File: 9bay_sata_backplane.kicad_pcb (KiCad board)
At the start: 2 copper layers, 115 x 58 mm, 57 parts, among them J1 Screw_Terminal_01x04, U1 SATA_Connector, U10 SATA_Data, U11 SATA_Data, U12 SATA_Data, U13 SATA_Data, U14 SATA_Data, U15 SATA_Data, U16 SATA_Data, U17 SATA_Data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

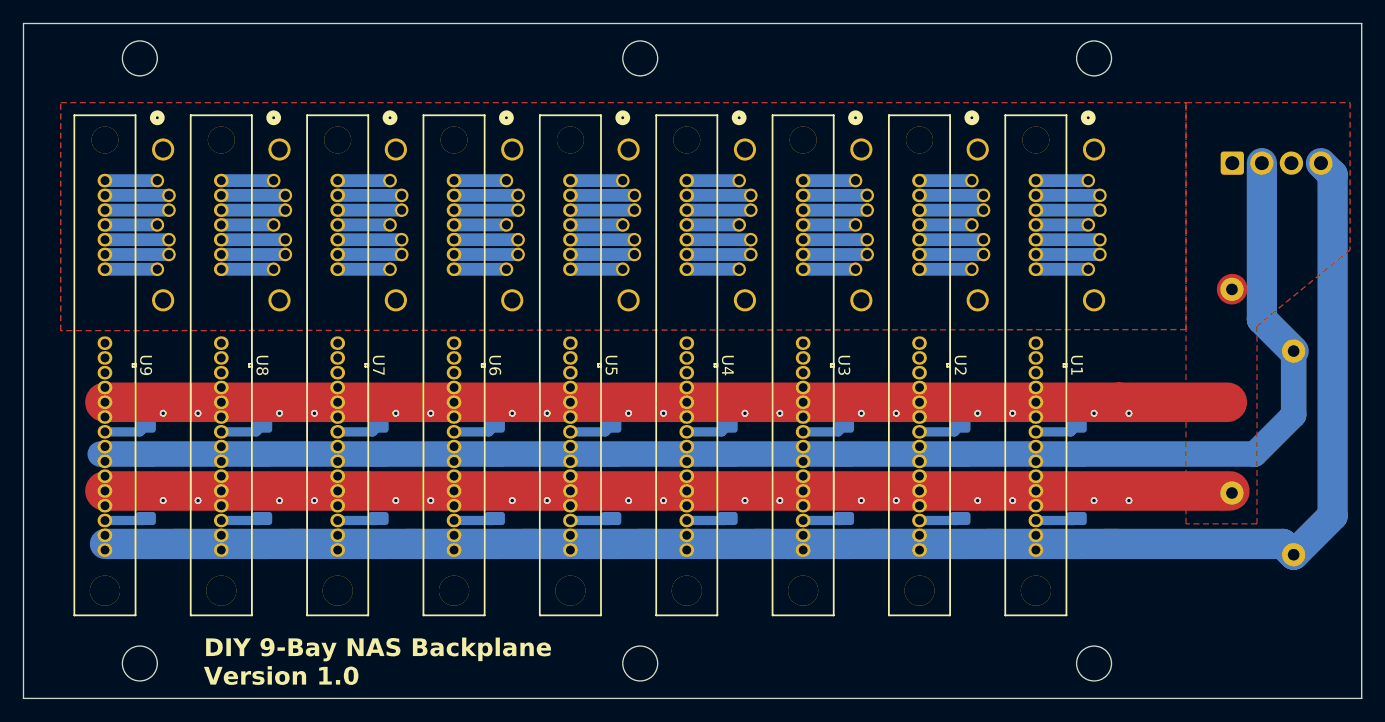
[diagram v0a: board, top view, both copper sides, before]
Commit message: DIY 9-Bay SATA Backplane v1.2
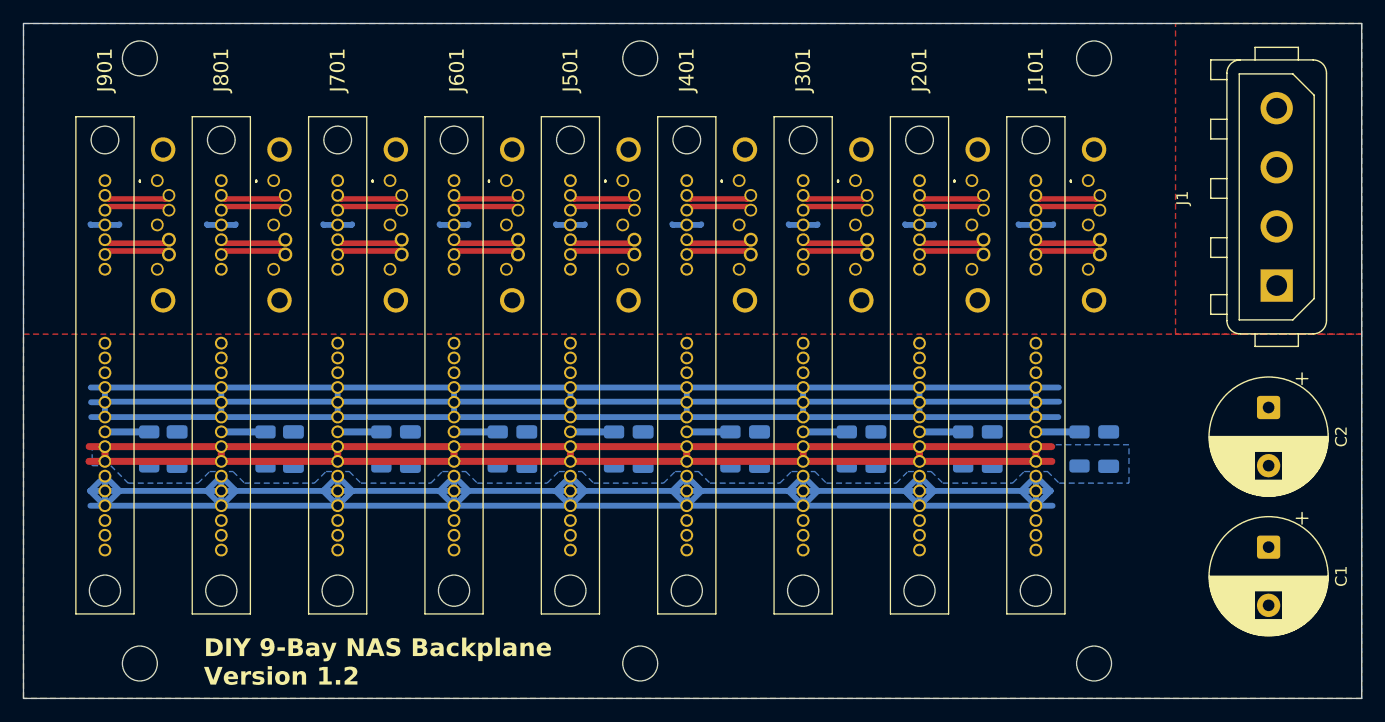
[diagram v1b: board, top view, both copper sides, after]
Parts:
- removed C10, C11, C12, C13, C14, C15, C16, C17, C18, C3, C4, C5, C6, C7, C8, C9: C_Small, Capacitor_SMD:C_1206_3216Metric
- removed C19, C20: C_Polarized_Small, Capacitor_THT:C_Radial_D16.0mm_H25.0mm_P7.50mm
- removed R1, R10, R11, R12, R13, R14, R15, R16, R17, R18, R2, R3, R4, R5, R6, R7, R8, R9: R_Small_US, Resistor_SMD:R_1206_3216Metric
- removed U1, U2, U3, U4, U5, U6, U7, U8, U9: SATA_Connector, Connector_SATA_SAS:CONN_877791001_MOL
- removed U10, U11, U12, U13, U14, U15, U16, U17, U18: SATA_Data, Connector_SATA_SAS:CONN_67800-8025_MOL
- added C1: 25v 560uf, Capacitor_THT:CP_Radial_D10.0mm_P5.00mm, F.Cu at (181.0, 103.0)
- added C201: 35v 10uf, Capacitor_SMD:C_1206_3216Metric, B.Cu at (157.2, 94.6)
- added C301: 35v 10uf, Capacitor_SMD:C_1206_3216Metric, B.Cu at (147.2, 94.6)
- added C401: 35v 10uf, Capacitor_SMD:C_1206_3216Metric, B.Cu at (137.2, 94.6)
- added C501: 35v 10uf, Capacitor_SMD:C_1206_3216Metric, B.Cu at (127.2, 94.6)
- added C601: 35v 10uf, Capacitor_SMD:C_1206_3216Metric, B.Cu at (117.2, 94.6)
- added C701: 35v 10uf, Capacitor_SMD:C_1206_3216Metric, B.Cu at (107.2, 94.6)
- added C801: 35v 10uf, Capacitor_SMD:C_1206_3216Metric, B.Cu at (97.2, 94.6)
- added C901: 35v 10uf, Capacitor_SMD:C_1206_3216Metric, B.Cu at (87.2, 94.6)
- added H1: MountingHole, MountingHole:MountingHole_3mm, F.Cu at (84.0, 61.0)
- added H2: MountingHole, MountingHole:MountingHole_3mm, F.Cu at (127.0, 61.0)
- added H3: MountingHole, MountingHole:MountingHole_3mm, F.Cu at (166.0, 61.0)
- added H4: MountingHole, MountingHole:MountingHole_3mm, F.Cu at (84.0, 113.0)
- added H5: MountingHole, MountingHole:MountingHole_3mm, F.Cu at (127.0, 113.0)
- added H6: MountingHole, MountingHole:MountingHole_3mm, F.Cu at (166.0, 113.0)
- added J101: 87779-1001, 87779-1001:877791001, F.Cu at (161.0, 71.5)
- added J102: 67800-8025, 67800-8025:678008025, B.Cu at (165.5, 75.3)
- added J201: 87779-1001, 87779-1001:877791001, F.Cu at (151.0, 71.5)
- added J202: 67800-8025, 67800-8025:678008025, B.Cu at (155.5, 75.3)
- added J301: 87779-1001, 87779-1001:877791001, F.Cu at (141.0, 71.5)
- added J302: 67800-8025, 67800-8025:678008025, B.Cu at (145.5, 75.3)
- added J401: 87779-1001, 87779-1001:877791001, F.Cu at (131.0, 71.5)
- added J402: 67800-8025, 67800-8025:678008025, B.Cu at (135.5, 75.3)
- added J501: 87779-1001, 87779-1001:877791001, F.Cu at (121.0, 71.5)
- added J502: 67800-8025, 67800-8025:678008025, B.Cu at (125.5, 75.3)
- added J601: 87779-1001, 87779-1001:877791001, F.Cu at (111.0, 71.5)
- added J602: 67800-8025, 67800-8025:678008025, B.Cu at (115.5, 75.3)
- added J701: 87779-1001, 87779-1001:877791001, F.Cu at (101.0, 71.5)
- added J702: 67800-8025, 67800-8025:678008025, B.Cu at (105.5, 75.3)
- added J801: 87779-1001, 87779-1001:877791001, F.Cu at (91.0, 71.5)
- added J802: 67800-8025, 67800-8025:678008025, B.Cu at (95.5, 75.3)
- added J901: 87779-1001, 87779-1001:877791001, F.Cu at (81.0, 71.5)
- added J902: 67800-8025, 67800-8025:678008025, B.Cu at (85.5, 75.3)
- added R101: 22ohm, Resistor_SMD:R_1206_3216Metric, B.Cu at (164.8, 94.6)
- added R201: 22ohm, Resistor_SMD:R_1206_3216Metric, B.Cu at (154.8, 94.6)
- added R301: 22ohm, Resistor_SMD:R_1206_3216Metric, B.Cu at (144.8, 94.6)
- added R401: 22ohm, Resistor_SMD:R_1206_3216Metric, B.Cu at (134.8, 94.6)
- added R501: 22ohm, Resistor_SMD:R_1206_3216Metric, B.Cu at (124.8, 94.6)
- added R601: 22ohm, Resistor_SMD:R_1206_3216Metric, B.Cu at (114.8, 94.6)
- added R701: 22ohm, Resistor_SMD:R_1206_3216Metric, B.Cu at (104.8, 94.6)
- added R801: 22ohm, Resistor_SMD:R_1206_3216Metric, B.Cu at (94.8, 94.6)
- added R901: 22ohm, Resistor_SMD:R_1206_3216Metric, B.Cu at (84.8, 94.6)
- C101: renamed from C1; value C_Small -> 35v 10uf
- C2: value C_Small -> 25v 560uf; footprint Capacitor_SMD:C_1206_3216Metric -> Capacitor_THT:CP_Radial_D10.0mm_P5.00mm; moved to F.Cu
- J1: value Screw_Terminal_01x04 -> HDD POWER; footprint TerminalBlock:TerminalBlock_Xinya_XY308-2.54-4P_1x04_P2.54mm_Horizontal -> Connector_TE-Connectivity:TE_MATE-N-LOK_350211-1_1x04_P5.08mm_Vertical; moved to F.Cu
- moved C2 16.5 mm to (181.0, 91.0)
- moved J1 11.2 mm to (181.7, 80.5), turned to 90 degrees
- moved C101 1.47 mm to (167.2, 94.6)
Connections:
- C2 pad 1: GND -> +5V
- C2 pad 2: +12V -> GND
- J1 pad 1: GND -> unconnected-(J1-Pin_1-Pad1)
- J1 pad 2: +5V -> GND
- J1 pad 4: +12V -> +5V
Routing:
- net GND: track 368.9 -> 548.4 mm, vias 36 -> 0
- net +12V: track 138.3 -> 0.00 mm
- net +5V: track 126.7 -> 176.9 mm
- net /SATA9 B-: track 0.00 -> 5.75 mm
- net /SATA9 A+: track 0.00 -> 5.75 mm
- net /SATA8 B-: track 0.00 -> 5.75 mm
- net /SATA8 A+: track 0.00 -> 5.75 mm
- net /SATA7 B-: track 0.00 -> 5.75 mm
- net /SATA7 A+: track 0.00 -> 5.75 mm
- net /SATA6 B-: track 0.00 -> 5.75 mm
- net /SATA6 A+: track 0.00 -> 5.75 mm
- net /SATA5 B-: track 0.00 -> 5.75 mm
- net /SATA5 A+: track 0.00 -> 5.75 mm
- net /SATA4 B-: track 0.00 -> 5.75 mm
- net /SATA4 A+: track 0.00 -> 5.75 mm
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- added copper zone on B.Cu, net +5V
- added copper zone on F.Cu, net +5V
- added copper zone on B.Cu, net GND
- removed copper zone on F.Cu, net GND
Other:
- outline, holes or cut-outs redrawn
- board text added: "DIY 9-Bay NAS Backplane Version 1.2"
- board text removed: "+"
- board text removed: "12V"
- board text removed: "5V"
- board text removed: "DIY 9-Bay NAS Backplane Version 1.0"
- board text removed: "G"
